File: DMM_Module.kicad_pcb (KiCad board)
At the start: 4 copper layers, 60 x 96 mm, 123 parts, among them J1 M20-7810245, J2 M20-7810245, J3 M20-7812045, J4 M20-7812045, J5 M20-7810245, J6 M20-7810245, K1 G6K-2F-Y-TR, K2 G6K-2F-Y-TR, K3 G6K-2F-Y-TR, K4 G6K-2F-Y-TR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

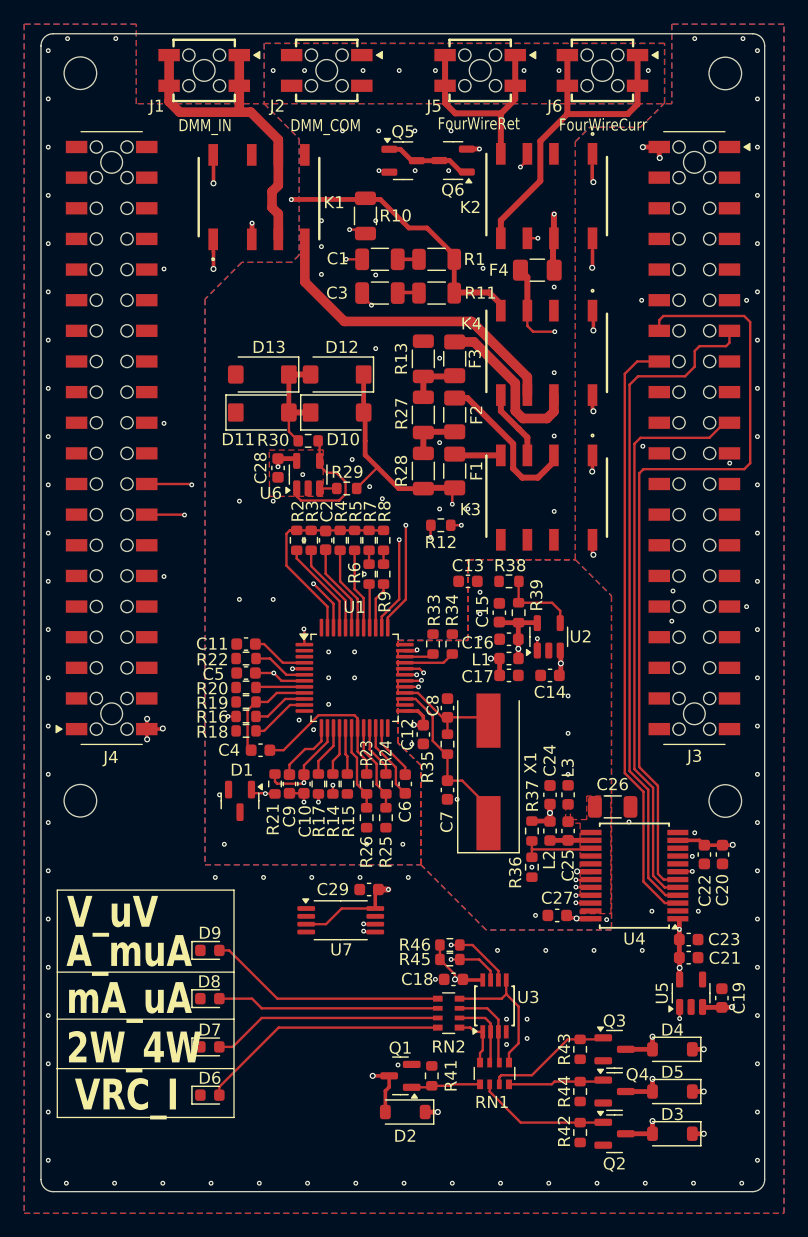
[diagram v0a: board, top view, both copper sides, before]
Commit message: Added GND vias for high current path
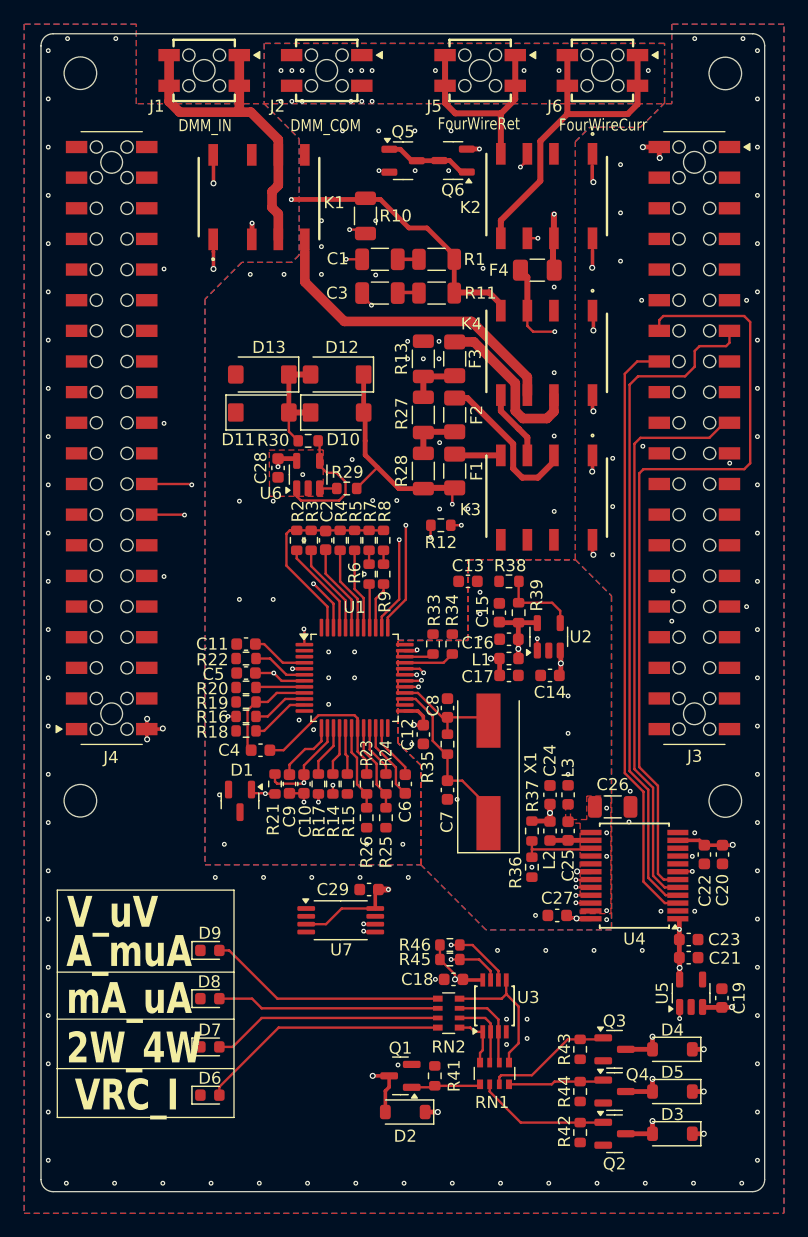
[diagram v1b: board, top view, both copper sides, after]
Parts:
- moved R41 0.25 mm to (169.9, 122.0)
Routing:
- net GNDA: vias 50 -> 63
- net GND: vias 97 -> 104
- net /Interface/GNDiso: vias 0 -> 4
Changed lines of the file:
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@@
 	(footprint "Resistor_SMD:R_0603_1608Metric"
 		(layer "F.Cu")
-		(at 169.695 121.99 90)
+		(at 169.945 121.99 90)
 		(descr "Resistor SMD 0603 (1608 Metric), square (rectangular) end terminal, IPC_7351 nominal, (Body size source: IPC-SM-782 page 72, https://www.pcb-3d.com/wordpress/wp-content/uploads/ipc-sm-782a_amendment_1_and_2.pdf), generated with kicad-footprint-generator")
 		(tags "resistor")
@@
 	)
 	(segment
-		(start 167.545 76.34)
-		(end 167.545 61.54)
+		(start 167.545 66.99)
+		(end 164.695 64.14)
 		(width 0.2)
 		(layer "In1.Cu")
@@
 	)
 	(segment
-		(start 164.695 58.69)
-		(end 164.695 58.09)
+		(start 167.545 76.34)
+		(end 167.545 66.99)
 		(width 0.2)
 		(layer "In1.Cu")
@@
 	)
 	(segment
-		(start 167.545 61.54)
-		(end 164.695 58.69)
+		(start 164.695 64.14)
+		(end 164.695 58.09)
 		(width 0.2)
 		(layer "In1.Cu")
@@
 	)
 	(via
+		(at 167.695 62.54)
+		(size 0.4)
+		(drill 0.2)
+		(layers "F.Cu" "B.Cu")
+		(free yes)
+		(net 11)
+	)
+	(via
 		(at 171.095 46.94)
 		(size 0.4)
@@
 	)
 	(via
-		(at 156.545 38.64)
+		(at 163.895 38.64)
 		(size 0.4)
 		(drill 0.2)
@@
 	)
 	(via
-		(at 160.545 51.09)
+		(at 157.195 38.64)
 		(size 0.4)
 		(drill 0.2)
@@
 	)
 	(via
-		(at 163.995 38.64)
+		(at 160.545 51.09)
 		(size 0.4)
 		(drill 0.2)
@@
 	)
 	(via
-		(at 164.545 73.14)
+		(at 164.795 74.29)
 		(size 0.4)
 		(drill 0.2)
@@
 	)
 	(via
-		(at 159.145 38.64)
+		(at 158.945 38.64)
 		(size 0.4)
 		(drill 0.2)
@@
 	)
 	(via
+		(at 158.095 41.19)
+		(size 0.4)
+		(drill 0.2)
+		(layers "F.Cu" "B.Cu")
+		(free yes)
+		(net 11)
+	)
+	(via
+		(at 164.745 41.19)
+		(size 0.4)
+		(drill 0.2)
+		(layers "F.Cu" "B.Cu")
+		(free yes)
+		(net 11)
+	)
+	(via
 		(at 159.895 93.29)
 		(size 0.4)
@@
 	)
 	(via
+		(at 157.445 55.54)
+		(size 0.4)
+		(drill 0.2)
+		(layers "F.Cu" "B.Cu")
+		(free yes)
+		(net 11)
+	)
+	(via
 		(at 163.295 88.99)
 		(size 0.4)
@@
 	)
 	(via
+		(at 162.995 41.19)
+		(size 0.4)
+		(drill 0.2)
+		(layers "F.Cu" "B.Cu")
+		(free yes)
+		(net 11)
+	)
+	(via
 		(at 172.695 74.99)
 		(size 0.4)
@@
 	)
 	(via
+		(at 170.295 61.09)
+		(size 0.4)
+		(drill 0.2)
+		(layers "F.Cu" "B.Cu")
+		(free yes)
+		(net 11)
+	)
+	(via
 		(at 177.345 38.64)
 		(size 0.4)
@@
 	)
 	(via
-		(at 179.845 63.69)
+		(at 154.645 55.54)
 		(size 0.4)
 		(drill 0.2)
@@
 	)
 	(via
-		(at 152.495 102.79)
+		(at 179.845 63.69)
 		(size 0.4)
 		(drill 0.2)
@@
 	)
 	(via
-		(at 166.995 38.64)
+		(at 152.495 102.79)
 		(size 0.4)
 		(drill 0.2)
@@
 	)
 	(via
-		(at 170.345 62.49)
+		(at 170.295 62.54)
 		(size 0.4)
 		(drill 0.2)
@@
 	)
 	(via
+		(at 163.895 41.19)
+		(size 0.4)
+		(drill 0.2)
+		(layers "F.Cu" "B.Cu")
+		(free yes)
+		(net 11)
+	)
+	(via
 		(at 165.045 55.59)
 		(size 0.4)
@@
 	)
 	(via
-		(at 165.595 74.14)
+		(at 166.795 74.29)
 		(size 0.4)
 		(drill 0.2)
@@
 	)
 	(via
+		(at 164.745 38.64)
+		(size 0.4)
+		(drill 0.2)
+		(layers "F.Cu" "B.Cu")
+		(free yes)
+		(net 11)
+	)
+	(via
 		(at 156.545 82.49)
 		(size 0.4)
@@
 	)
 	(via
+		(at 162.995 38.64)
+		(size 0.4)
+		(drill 0.2)
+		(layers "F.Cu" "B.Cu")
+		(free yes)
+		(net 11)
+	)
+	(via
+		(at 158.945 41.19)
+		(size 0.4)
+		(drill 0.2)
+		(layers "F.Cu" "B.Cu")
+		(free yes)
+		(net 11)
+	)
+	(via
 		(at 160.545 53.24)
 		(size 0.4)
@@
 	)
 	(via
+		(at 158.095 38.64)
+		(size 0.4)
+		(drill 0.2)
+		(layers "F.Cu" "B.Cu")
+		(free yes)
+		(net 11)
+	)
+	(via
 		(at 171.295 43.64)
 		(size 0.4)
@@
 	)
 	(via
-		(at 165.045 61.69)
+		(at 168.995 62.54)
+		(size 0.4)
+		(drill 0.2)
+		(layers "F.Cu" "B.Cu")
+		(free yes)
+		(net 11)
+	)
+	(via
+		(at 167.695 61.09)
+		(size 0.4)
+		(drill 0.2)
+		(layers "F.Cu" "B.Cu")
+		(free yes)
+		(net 11)
+	)
+	(via
+		(at 157.195 41.19)
 		(size 0.4)
 		(drill 0.2)
@@
 	)
 	(via
+		(at 186.145 98.39)
+		(size 0.4)
+		(drill 0.2)
+		(layers "F.Cu" "B.Cu")
+		(free yes)
+		(net 15)
+	)
+	(via
 		(at 191.495 35.99)
 		(size 0.4)
@@
 	)
 	(via
-		(at 187.945 108.34)
+		(at 188.695 108.34)
+		(size 0.4)
+		(drill 0.2)
+		(layers "F.Cu" "B.Cu")
+		(free yes)
+		(net 15)
+	)
+	(via
+		(at 185.345 50.44)
+		(size 0.4)
+		(drill 0.2)
+		(layers "F.Cu" "B.Cu")
+		(free yes)
+		(net 15)
+	)
+	(via
+		(at 185.345 54.44)
 		(size 0.4)
 		(drill 0.2)
@@
 	)
 	(via
+		(at 185.345 46.44)
+		(size 0.4)
+		(drill 0.2)
+		(layers "F.Cu" "B.Cu")
+		(free yes)
+		(net 15)
+	)
+	(via
 		(at 196.695 124.99)
 		(size 0.4)
@@
 	)
 	(via
+		(at 184.695 74.79)
+		(size 0.4)
+		(drill 0.2)
+		(layers "F.Cu" "B.Cu")
+		(free yes)
+		(net 15)
+	)
+	(via
 		(at 196.695 120.99)
 		(size 0.4)
@@
 	)
 	(via
-		(at 191.795 108.34)
+		(at 191.495 108.34)
 		(size 0.4)
 		(drill 0.2)
@@
 	)
 	(via
+		(at 184.695 70.79)
+		(size 0.4)
+		(drill 0.2)
+		(layers "F.Cu" "B.Cu")
+		(free yes)
+		(net 15)
+	)
+	(via
 		(at 191.295 103.79)
 		(size 0.4)
@@
 	)
 	(via
+		(at 184.695 78.79)
+		(size 0.4)
+		(drill 0.2)
+		(layers "F.Cu" "B.Cu")
+		(free yes)
+		(net 15)
+	)
+	(via
 		(at 191.495 101.84)
 		(size 0.4)
@@
 	)
 	(segment
-		(start 171.395 122.69)
-		(end 171.27 122.815)
-		(width 0.2)
-		(layer "F.Cu")
-		(net 106)
-	)
-	(segment
-		(start 173.695 122.69)
-		(end 171.395 122.69)
+		(start 173.57 122.815)
+		(end 169.695 122.815)
 		(width 0.2)
 		(layer "F.Cu")
@@
 	)
 	(segment
-		(start 171.27 122.815)
-		(end 169.695 122.815)
+		(start 168.0325 122.94)
+		(end 169.57 122.94)
 		(width 0.2)
 		(layer "F.Cu")
@@
 	)
 	(segment
-		(start 168.0325 122.94)
-		(end 169.57 122.94)
+		(start 173.695 122.69)
+		(end 173.57 122.815)
 		(width 0.2)
 		(layer "F.Cu")
@@
 		(net 156)
 	)
+	(via
+		(at 184.195 103.79)
+		(size 0.4)
+		(drill 0.2)
+		(layers "F.Cu" "B.Cu")
+		(free yes)
+		(net 160)
+	)
+	(via
+		(at 184.195 108.29)
+		(size 0.4)
+		(drill 0.2)
+		(layers "F.Cu" "B.Cu")
+		(free yes)
+		(net 160)
+	)
+	(via
+		(at 184.195 101.84)
+		(size 0.4)
+		(drill 0.2)
+		(layers "F.Cu" "B.Cu")
+		(free yes)
+		(net 160)
+	)
+	(via
+		(at 184.195 99.79)
+		(size 0.4)
+		(drill 0.2)
+		(layers "F.Cu" "B.Cu")
+		(free yes)
+		(net 160)
+	)
 	(segment

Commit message: Relay traces were aligned
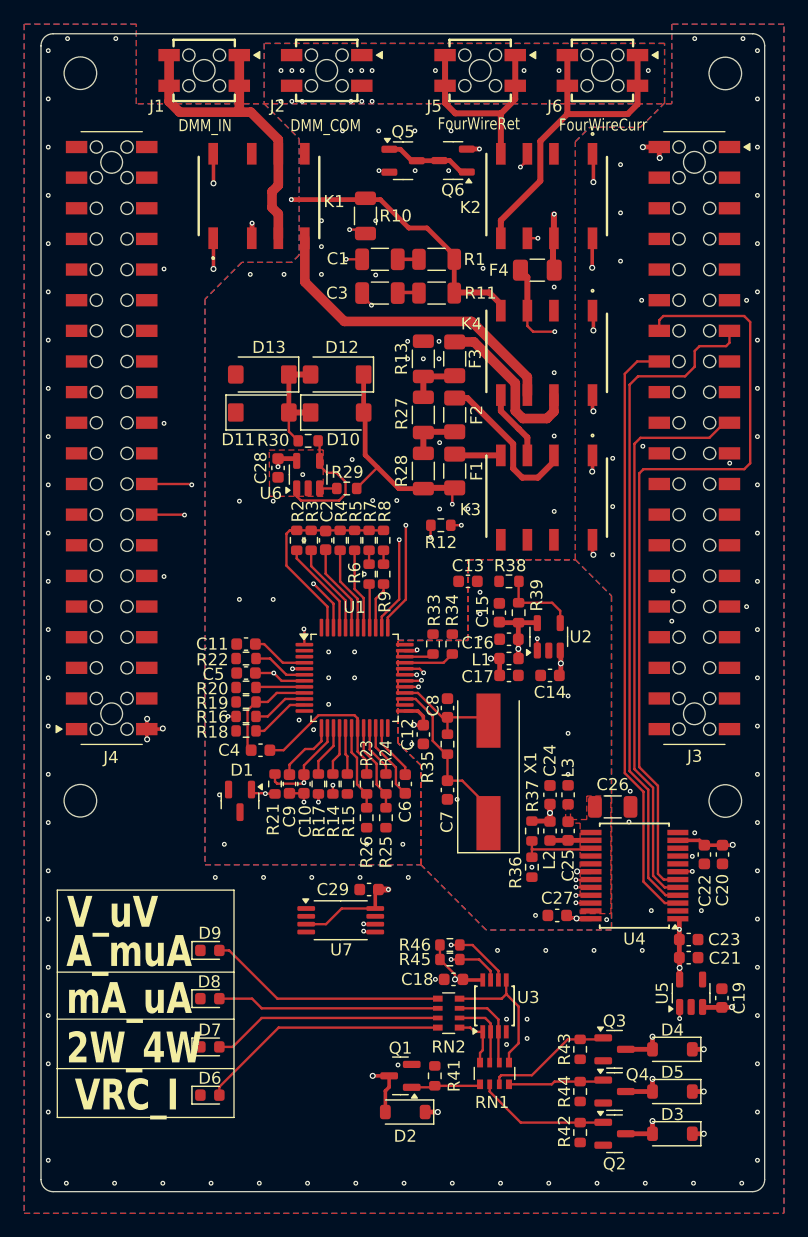
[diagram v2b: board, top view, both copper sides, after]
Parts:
- moved K1 0.09 mm to (150.4, 49.0)
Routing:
- net 5V: track 23.3 -> 25.3 mm
- net Net-(U1B-XOUT): track 15.7 -> 14.5 mm
- net /DMM DAQ/CurrentIn: track 25.7 -> 26.8 mm
- net /Power/RELAY1: track 78.9 -> 79.9 mm
- net /Interface/GNDiso: vias 4 -> 0
